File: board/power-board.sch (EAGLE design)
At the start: 446 parts, among them J1 H1, J2 H2, J6 DF13-8P-1.25DS, J7 DF13-10P-1.25DS, J8 DF13-4P-1.25DS, J9 DF13-4P-1.25DS, Q3 SI7288, U1 INA214DCK, U10 INA214DCK, U11 INA214DCK, U12 INA214DCK, U13 MCP6561T-E/LT, U14 INA214DCK, U15 SN74AUP1G00DCK, U16 SN74LVC1G373DCK, U17 NTHD4508NT1, U18 MCP6561T-E/LT, U19 INA214DCK, U2 INA214DCK, U20 SN74AUP1G00DCK, U21 SN74LVC1G373DCK, U22 NTHD4508NT1, U23 MCP6561T-E/LT, U24 INA214DCK, U25 SN74AUP1G00DCK, U26 SN74LVC1G373DCK, U27 NTHD4508NT1, U28 MCP6561T-E/LT, U29 INA214DCK, U3 INA214DCK, U30 SN74AUP1G00DCK, U31 SN74LVC1G373DCK, U32 NTHD4508NT1, U33 MCP6561T-E/LT, U34 INA214DCK, U35 SN74AUP1G00DCK, U36 SN74LVC1G373DCK, U37 NTHD4508NT1, U38 MCP6561T-E/LT, U39 INA214DCK, U4 INA214DCK, U40 SN74AUP1T08DCK, U41 SN74LVC1G373DCK, U42 FDS8858CZ, U43 TLV3491AIDBV, U44 TPS62132RGT, U45 FDS8858CZ, U46 TLV3491AIDBV, U47 TPS62133RGT, U48 FDS8858CZ, U49 MSP430F2132, U5 INA214DCK, U50 ADG732, U51 SPV1040T, U52 SPV1040T, U53 BQ24650_RVA_16, U54 INA214DCK, U55 SPV1040T, U56 SPV1040T, U57 SPV1040T, U58 SPV1040T, U6 INA214DCK, U7 INA214DCK, U8 INA214DCK, U9 INA214DCK, X1 32.768k

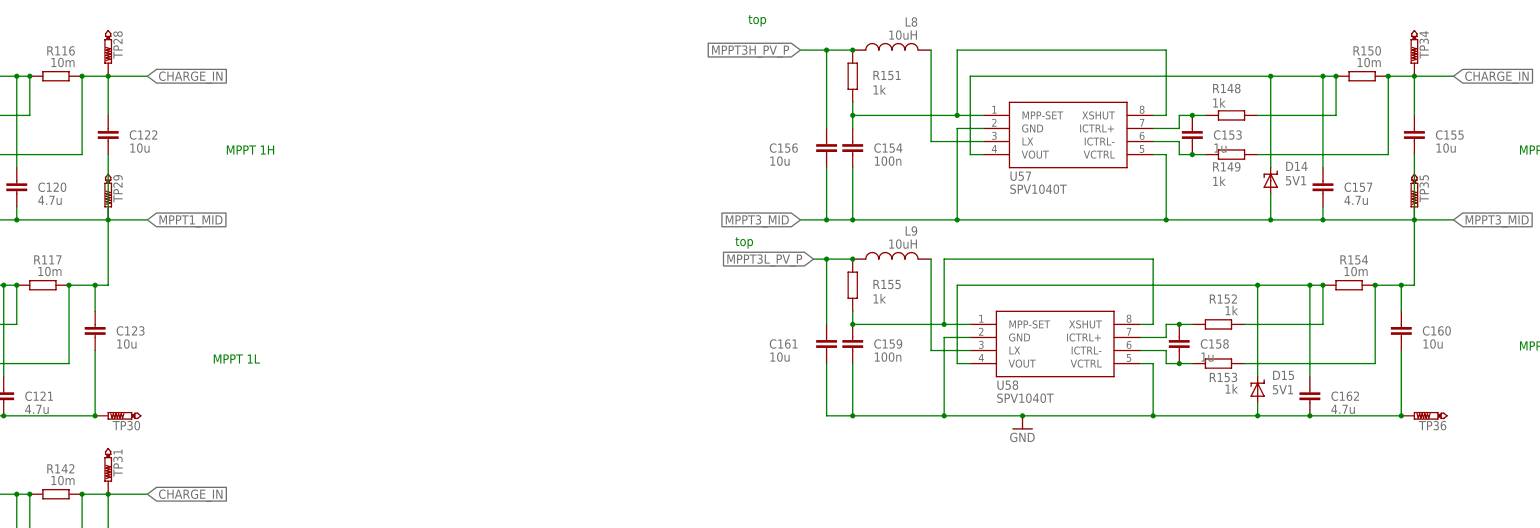
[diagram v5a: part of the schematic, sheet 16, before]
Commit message: no airwires
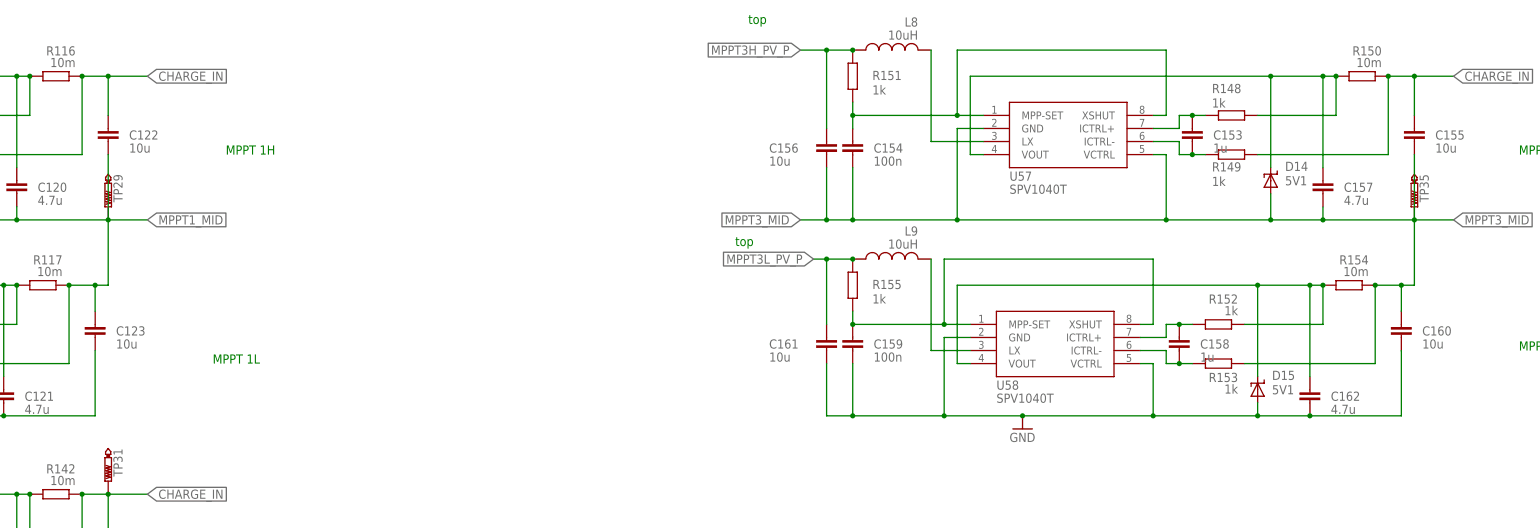
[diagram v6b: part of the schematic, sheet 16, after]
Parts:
- removed TP28, TP30, TP34, TP36: PTR1TP09R, testpad:PTR1TP09R
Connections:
- net CHARGE_IN: no longer TP28.TP, TP34.TP
- net GND: no longer TP30.TP, TP36.TP
- net MPPT2L_PV_P: no longer R27.2
- net MPPT2_MID: now also R27.2
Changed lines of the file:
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@@
 <part name="TP26" library="testpad" deviceset="PTR1" device="TP09R"/>
 <part name="TP27" library="testpad" deviceset="PTR1" device="TP09R"/>
-<part name="TP28" library="testpad" deviceset="PTR1" device="TP09R"/>
 <part name="TP29" library="testpad" deviceset="PTR1" device="TP09R"/>
-<part name="TP30" library="testpad" deviceset="PTR1" device="TP09R"/>
 <part name="U55" library="gdp_pss_library" deviceset="SPV1040" device="T"/>
 <part name="C143" library="rcl" deviceset="C-EU" device="C0603K" value="1u"/>
@@
 <part name="L9" library="gdp_pss_library" deviceset="MSS7341" device="" value="10uH"/>
 <part name="GND130" library="supply1" deviceset="GND" device=""/>
-<part name="TP34" library="testpad" deviceset="PTR1" device="TP09R"/>
 <part name="TP35" library="testpad" deviceset="PTR1" device="TP09R"/>
-<part name="TP36" library="testpad" deviceset="PTR1" device="TP09R"/>
 </parts>
 <sheets>
@@
 <net name="MPPT2L_PV_P" class="0">
 <segment>
-<label x="38.1" y="104.14" size="1.778" layer="95" rot="R180" xref="yes"/>
-<pinref part="R27" gate="G$1" pin="2"/>
-<wire x1="40.64" y1="104.14" x2="38.1" y2="104.14" width="0.1524" layer="91"/>
-<wire x1="40.64" y1="101.6" x2="40.64" y2="104.14" width="0.1524" layer="91"/>
-</segment>
-<segment>
 <label x="38.1" y="157.48" size="1.778" layer="95" rot="R180" xref="yes"/>
 <pinref part="R25" gate="G$1" pin="2"/>
@@
 </segment>
 </net>
+<net name="MPPT2_MID" class="0">
+<segment>
+<label x="38.1" y="104.14" size="1.778" layer="95" rot="R180" xref="yes"/>
+<pinref part="R27" gate="G$1" pin="2"/>
+<wire x1="40.64" y1="104.14" x2="38.1" y2="104.14" width="0.1524" layer="91"/>
+<wire x1="40.64" y1="101.6" x2="40.64" y2="104.14" width="0.1524" layer="91"/>
+</segment>
+</net>
 </nets>
 </sheet>
@@
 </instance>
 <instance part="GND106" gate="1" x="76.2" y="88.9"/>
-<instance part="TP28" gate="G$1" x="152.4" y="160.02" rot="R180"/>
 <instance part="TP29" gate="G$1" x="152.4" y="132.08" rot="R180"/>
-<instance part="TP30" gate="G$1" x="152.4" y="91.44" rot="R90"/>
 <instance part="U55" gate="G$1" x="83.82" y="66.04" smashed="yes">
 <attribute name="NAME" x="73.66" y="55.88" size="1.778" layer="95"/>
@@
 </instance>
 <instance part="GND130" gate="1" x="330.2" y="88.9"/>
-<instance part="TP34" gate="G$1" x="406.4" y="160.02" rot="R180"/>
 <instance part="TP35" gate="G$1" x="406.4" y="132.08" rot="R180"/>
-<instance part="TP36" gate="G$1" x="406.4" y="91.44" rot="R90"/>
 </instances>
 <busses>
@@
 <wire x1="101.6" y1="101.6" x2="99.06" y2="101.6" width="0.1524" layer="91"/>
 <wire x1="101.6" y1="101.6" x2="101.6" y2="91.44" width="0.1524" layer="91"/>
-<pinref part="TP30" gate="G$1" pin="TP"/>
-<junction x="149.86" y="91.44"/>
 </segment>
 <segment>
@@
 <wire x1="355.6" y1="101.6" x2="353.06" y2="101.6" width="0.1524" layer="91"/>
 <wire x1="355.6" y1="101.6" x2="355.6" y2="91.44" width="0.1524" layer="91"/>
-<pinref part="TP36" gate="G$1" pin="TP"/>
-<junction x="403.86" y="91.44"/>
 </segment>
 </net>
@@
 <junction x="147.32" y="157.48"/>
 <junction x="152.4" y="157.48"/>
-<pinref part="TP28" gate="G$1" pin="TP"/>
 </segment>
 <segment>
@@
 <junction x="401.32" y="157.48"/>
 <junction x="406.4" y="157.48"/>
-<pinref part="TP34" gate="G$1" pin="TP"/>
 </segment>
 </net>

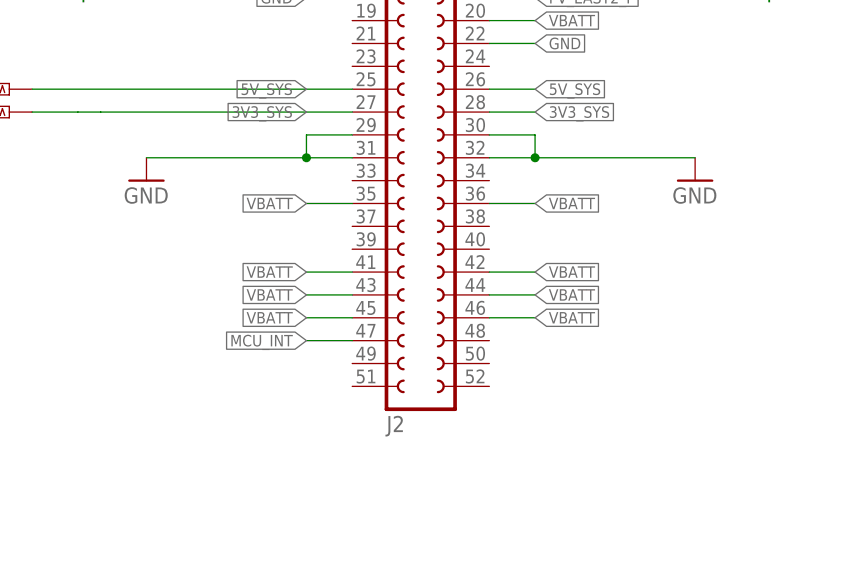
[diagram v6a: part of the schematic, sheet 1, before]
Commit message: separating vbat/charge. routing improvements for 3.3/5V regs
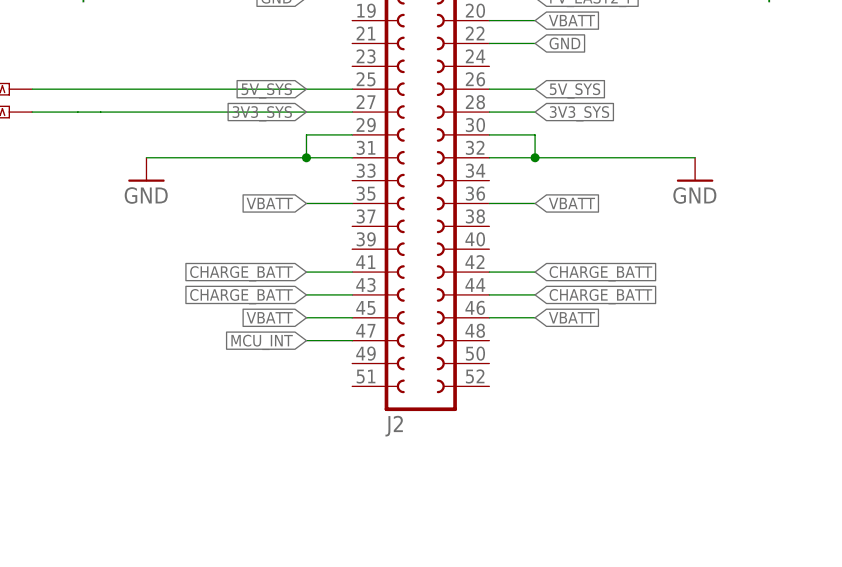
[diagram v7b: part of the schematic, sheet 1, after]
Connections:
- new net CHARGE_BATT: C142.1, J2.41, J2.42, J2.43, J2.44, R132.2, R137.2, U54.IN-
- net VBATT: no longer C142.1, J2.41, J2.42, J2.43, J2.44, R132.2, R137.2, U54.IN-
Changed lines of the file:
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@@
 <net name="VBATT" class="0">
 <segment>
-<pinref part="J2" gate="G$1" pin="42"/>
-<wire x1="200.66" y1="114.3" x2="195.58" y2="114.3" width="0.1524" layer="91"/>
-<label x="200.66" y="114.3" size="1.27" layer="95" xref="yes"/>
-</segment>
-<segment>
-<pinref part="J2" gate="G$1" pin="44"/>
-<wire x1="195.58" y1="111.76" x2="200.66" y2="111.76" width="0.1524" layer="91"/>
-<label x="200.66" y="111.76" size="1.27" layer="95" xref="yes"/>
-</segment>
-<segment>
-<pinref part="J2" gate="G$1" pin="41"/>
-<wire x1="175.26" y1="114.3" x2="180.34" y2="114.3" width="0.1524" layer="91"/>
-<label x="175.26" y="114.3" size="1.27" layer="95" rot="R180" xref="yes"/>
-</segment>
-<segment>
-<pinref part="J2" gate="G$1" pin="43"/>
-<wire x1="175.26" y1="111.76" x2="180.34" y2="111.76" width="0.1524" layer="91"/>
-<label x="175.26" y="111.76" size="1.27" layer="95" rot="R180" xref="yes"/>
-</segment>
-<segment>
 <pinref part="J2" gate="G$1" pin="35"/>
 <wire x1="180.34" y1="121.92" x2="175.26" y2="121.92" width="0.1524" layer="91"/>
@@
 </segment>
 </net>
+<net name="CHARGE_BATT" class="0">
+<segment>
+<pinref part="J2" gate="G$1" pin="41"/>
+<wire x1="180.34" y1="114.3" x2="175.26" y2="114.3" width="0.1524" layer="91"/>
+<label x="175.26" y="114.3" size="1.27" layer="95" rot="R180" xref="yes"/>
+</segment>
+<segment>
+<pinref part="J2" gate="G$1" pin="43"/>
+<wire x1="175.26" y1="111.76" x2="180.34" y2="111.76" width="0.1524" layer="91"/>
+<label x="175.26" y="111.76" size="1.27" layer="95" rot="R180" xref="yes"/>
+</segment>
+<segment>
+<pinref part="J2" gate="G$1" pin="42"/>
+<wire x1="195.58" y1="114.3" x2="200.66" y2="114.3" width="0.1524" layer="91"/>
+<label x="200.66" y="114.3" size="1.27" layer="95" xref="yes"/>
+</segment>
+<segment>
+<pinref part="J2" gate="G$1" pin="44"/>
+<wire x1="200.66" y1="111.76" x2="195.58" y2="111.76" width="0.1524" layer="91"/>
+<label x="200.66" y="111.76" size="1.27" layer="95" xref="yes"/>
+</segment>
+</net>
 </nets>
 </sheet>
@@
 </segment>
 </net>
-<net name="VBATT" class="0">
-<segment>
-<pinref part="U54" gate="G$1" pin="IN-"/>
-<wire x1="177.8" y1="134.62" x2="175.26" y2="134.62" width="0.1524" layer="91"/>
-<wire x1="175.26" y1="134.62" x2="175.26" y2="154.94" width="0.1524" layer="91"/>
-<pinref part="R132" gate="G$1" pin="2"/>
-<wire x1="175.26" y1="154.94" x2="172.72" y2="154.94" width="0.1524" layer="91"/>
-<wire x1="175.26" y1="154.94" x2="215.9" y2="154.94" width="0.1524" layer="91"/>
-<junction x="175.26" y="154.94"/>
-<label x="215.9" y="154.94" size="1.778" layer="95" xref="yes"/>
-</segment>
-</net>
 <net name="CHARGE_OUT" class="0">
 <segment>
@@
 </segment>
 </net>
+<net name="CHARGE_BATT" class="0">
+<segment>
+<pinref part="U54" gate="G$1" pin="IN-"/>
+<wire x1="177.8" y1="134.62" x2="175.26" y2="134.62" width="0.1524" layer="91"/>
+<wire x1="175.26" y1="134.62" x2="175.26" y2="154.94" width="0.1524" layer="91"/>
+<pinref part="R132" gate="G$1" pin="2"/>
+<wire x1="175.26" y1="154.94" x2="172.72" y2="154.94" width="0.1524" layer="91"/>
+<wire x1="175.26" y1="154.94" x2="215.9" y2="154.94" width="0.1524" layer="91"/>
+<junction x="175.26" y="154.94"/>
+<label x="215.9" y="154.94" size="1.778" layer="95" xref="yes"/>
+</segment>
+</net>
 </nets>
 </sheet>
@@
 </segment>
 </net>
-<net name="VBATT" class="0">
-<segment>
-<pinref part="R137" gate="G$1" pin="2"/>
-<wire x1="83.82" y1="20.32" x2="71.12" y2="20.32" width="0.1524" layer="91"/>
-<wire x1="71.12" y1="20.32" x2="66.04" y2="20.32" width="0.1524" layer="91"/>
-<junction x="71.12" y="20.32"/>
-<pinref part="C142" gate="G$1" pin="1"/>
-<wire x1="71.12" y1="17.78" x2="71.12" y2="20.32" width="0.1524" layer="91"/>
-<label x="83.82" y="20.32" size="1.778" layer="95" xref="yes"/>
-</segment>
-</net>
 <net name="N$762" class="0">
 <segment>
@@
 </segment>
 </net>
+<net name="CHARGE_BATT" class="0">
+<segment>
+<pinref part="R137" gate="G$1" pin="2"/>
+<wire x1="83.82" y1="20.32" x2="71.12" y2="20.32" width="0.1524" layer="91"/>
+<wire x1="71.12" y1="20.32" x2="66.04" y2="20.32" width="0.1524" layer="91"/>
+<junction x="71.12" y="20.32"/>
+<pinref part="C142" gate="G$1" pin="1"/>
+<wire x1="71.12" y1="17.78" x2="71.12" y2="20.32" width="0.1524" layer="91"/>
+<label x="83.82" y="20.32" size="1.778" layer="95" xref="yes"/>
+</segment>
+</net>

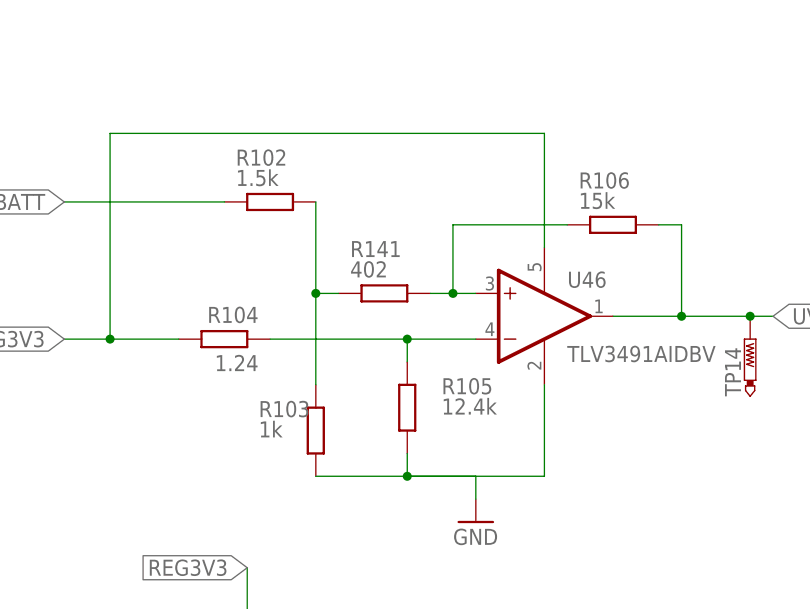
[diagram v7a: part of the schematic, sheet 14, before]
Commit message: updating component values
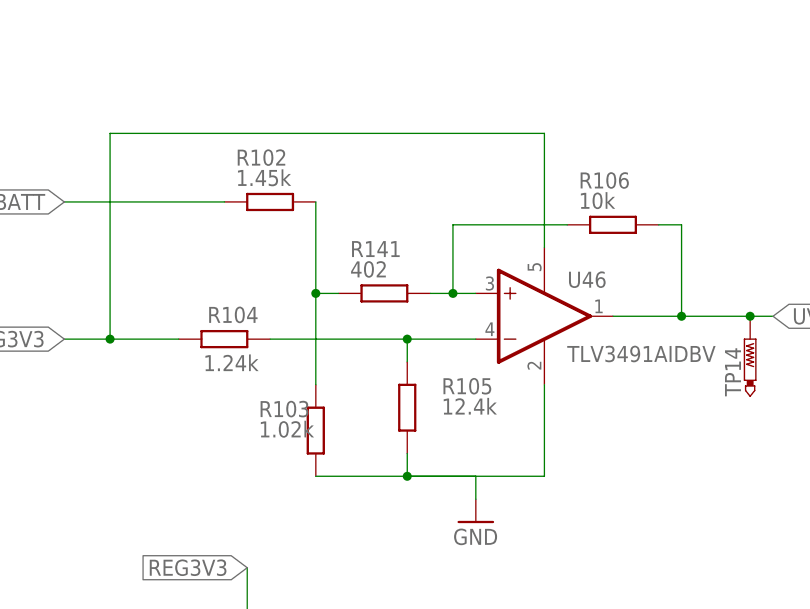
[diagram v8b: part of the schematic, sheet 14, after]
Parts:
- R102, R95: value 1.5k -> 1.45k
- R103, R96: value 1k -> 1.02k
- R104: value 1.24 -> 1.24k
- R106, R99: value 15k -> 10k
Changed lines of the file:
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@@
 <part name="C102" library="rcl" deviceset="C-EU" device="C1210" value="22u"/>
 <part name="L1" library="gdp_pss_library" deviceset="VISHAY-INDUCTOR" device="" value="2.2u"/>
-<part name="R95" library="rcl" deviceset="R-EU_" device="R0603" value="1.5k"/>
-<part name="R96" library="rcl" deviceset="R-EU_" device="R0603" value="1k"/>
+<part name="R95" library="rcl" deviceset="R-EU_" device="R0603" value="1.45k"/>
+<part name="R96" library="rcl" deviceset="R-EU_" device="R0603" value="1.02k"/>
 <part name="U43" library="tomparts" deviceset="TLV3491" device="AIDBV"/>
 <part name="R98" library="rcl" deviceset="R-EU_" device="R0603" value="12.4k"/>
 <part name="R97" library="rcl" deviceset="R-EU_" device="R0603" value="1.24k"/>
-<part name="R99" library="rcl" deviceset="R-EU_" device="R0603" value="15k"/>
+<part name="R99" library="rcl" deviceset="R-EU_" device="R0603" value="10k"/>
 <part name="C98" library="rcl" deviceset="C-EU" device="C0603" value="100n"/>
 <part name="GND86" library="supply1" deviceset="GND" device=""/>
@@
 <part name="C109" library="rcl" deviceset="C-EU" device="C1210" value="22u"/>
 <part name="L2" library="gdp_pss_library" deviceset="VISHAY-INDUCTOR" device="" value="2.2u"/>
-<part name="R102" library="rcl" deviceset="R-EU_" device="R0603" value="1.5k"/>
-<part name="R103" library="rcl" deviceset="R-EU_" device="R0603" value="1k"/>
+<part name="R102" library="rcl" deviceset="R-EU_" device="R0603" value="1.45k"/>
+<part name="R103" library="rcl" deviceset="R-EU_" device="R0603" value="1.02k"/>
 <part name="U46" library="tomparts" deviceset="TLV3491" device="AIDBV"/>
 <part name="R105" library="rcl" deviceset="R-EU_" device="R0603" value="12.4k"/>
-<part name="R104" library="rcl" deviceset="R-EU_" device="R0603" value="1.24"/>
-<part name="R106" library="rcl" deviceset="R-EU_" device="R0603" value="15k"/>
+<part name="R104" library="rcl" deviceset="R-EU_" device="R0603" value="1.24k"/>
+<part name="R106" library="rcl" deviceset="R-EU_" device="R0603" value="10k"/>
 <part name="C105" library="rcl" deviceset="C-EU" device="C0603" value="100n"/>
 <part name="GND94" library="supply1" deviceset="GND" device=""/>
